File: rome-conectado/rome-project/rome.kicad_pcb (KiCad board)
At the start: 2 copper layers, 109.2 x 83.8 mm, 19 parts, among them J1 Screw_Terminal_01x02, J2 Conn_02x04_Counter_Clockwise, U3 L7805

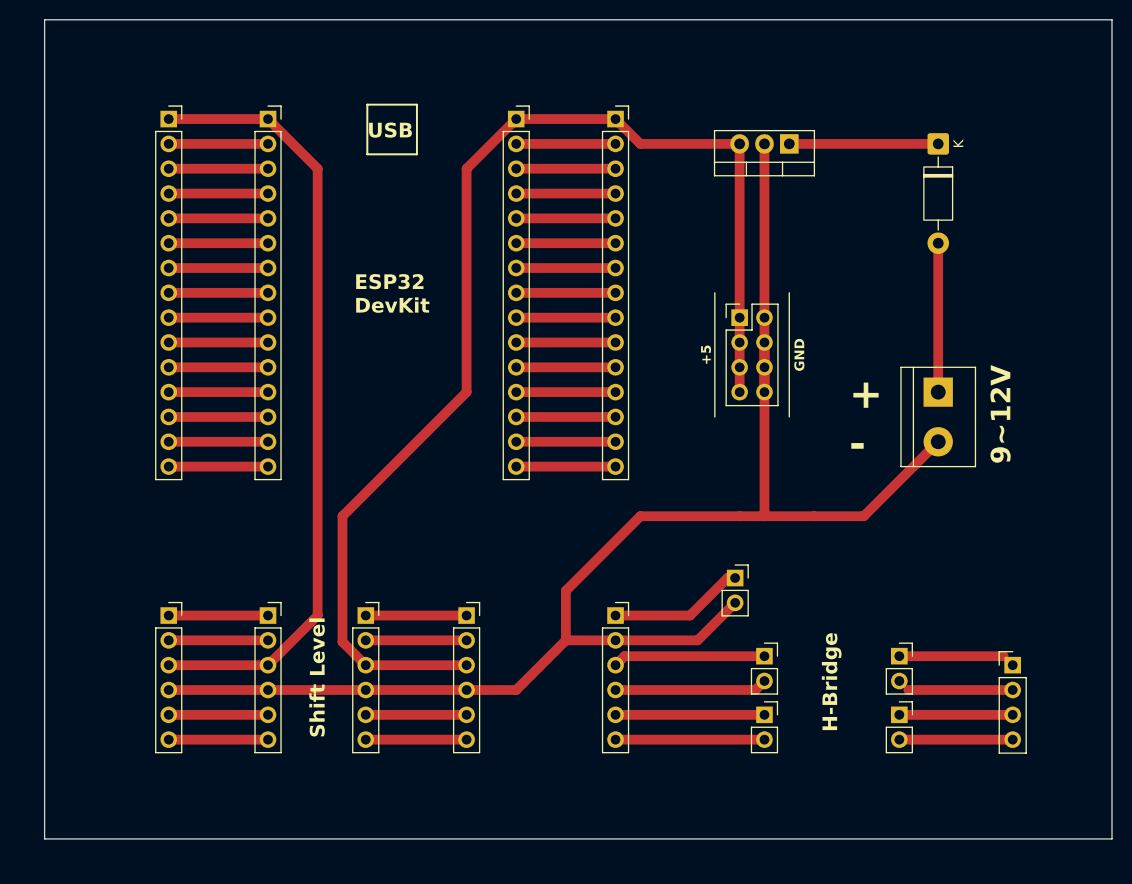
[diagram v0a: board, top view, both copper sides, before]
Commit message: Add ROSIE logo at the PCB
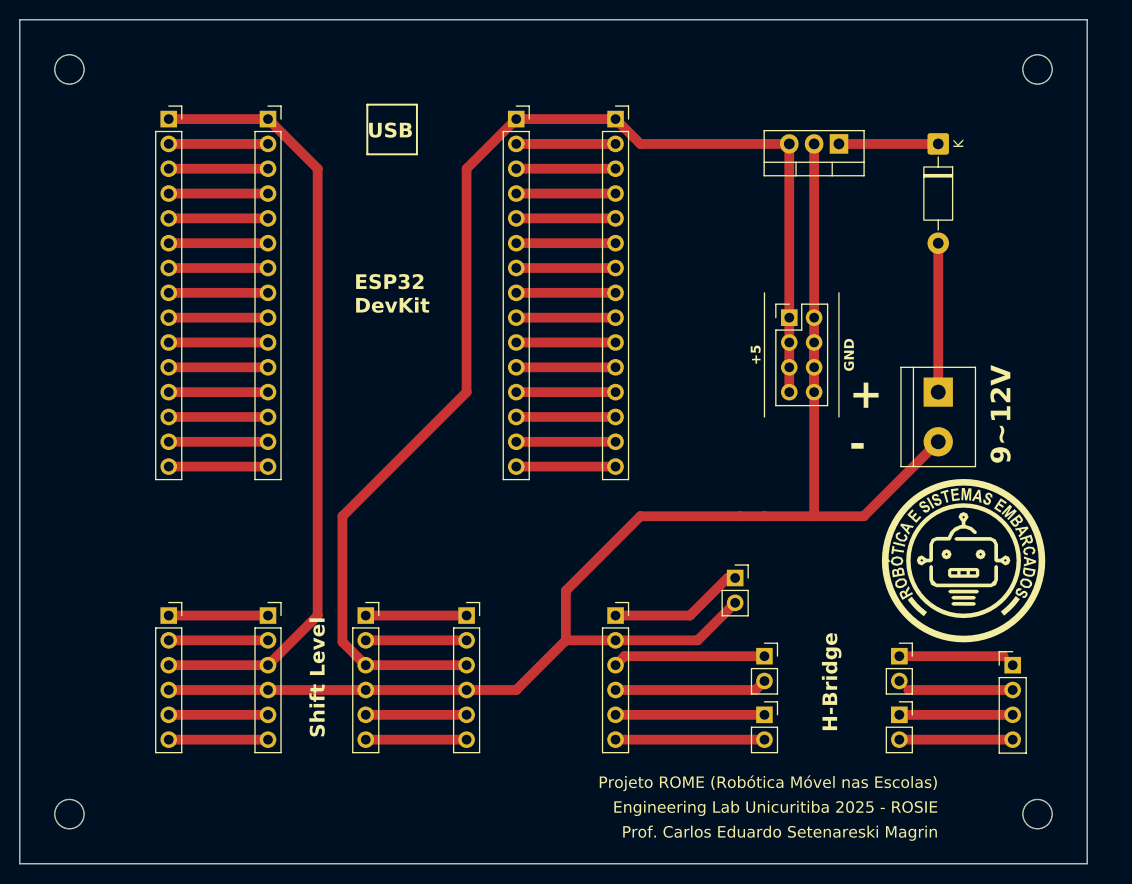
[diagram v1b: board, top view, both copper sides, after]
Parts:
- added UNK_HOLE_1: , dummyfp1, F.Cu at (94.0, 144.8)
- added UNK_HOLE_1: , dummyfp1, F.Cu at (94.0, 68.6)
- added UNK_HOLE_1: , dummyfp1, F.Cu at (193.0, 144.8)
- added UNK_HOLE_1: , dummyfp1, F.Cu at (193.0, 68.6)
- added svg2mod: G***, logo:logo_rosie, F.Cu at (176.8, 110.3)
- moved U3 5.08 mm to (172.7, 76.2)
- moved J2 5.08 mm to (167.6, 94.0)
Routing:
- net Net-(D3-K): track 15.2 -> 10.2 mm
- net +5V: track 123.9 -> 128.9 mm
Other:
- board size 109.2 x 83.8 mm -> 109.2 x 86.4 mm
- board text added: "Engineering Lab Unicuritiba 2025 - ROSIE"
- board text added: "Prof. Carlos Eduardo Setenareski Magrin"
- board text added: "Projeto ROME (Robótica Móvel nas Escolas)"
